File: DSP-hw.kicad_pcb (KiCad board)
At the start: 2 copper layers, 0 parts

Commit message: Iniziata un po la schematica
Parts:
- added C1: 100n, Capacitor_SMD:C_0603_1608Metric, F.Cu at (136.6, 67.8)
- added C10: 10u, Capacitor_SMD:C_0603_1608Metric, F.Cu at (136.6, 90.3)
- added C11: 1u, Capacitor_SMD:C_0603_1608Metric, F.Cu at (136.6, 92.9)
- added C12: 100n, Capacitor_SMD:C_0603_1608Metric, F.Cu at (136.6, 95.4)
- added C13: 10u, Capacitor_SMD:C_0603_1608Metric, F.Cu at (140.6, 67.8)
- added C14: 100n, Capacitor_SMD:C_0603_1608Metric, F.Cu at (140.6, 70.3)
- added C15: 10u, Capacitor_SMD:C_0603_1608Metric, F.Cu at (140.6, 72.8)
- added C16: 100n, Capacitor_SMD:C_0603_1608Metric, F.Cu at (140.6, 75.3)
- added C17: 10u, Capacitor_SMD:C_0603_1608Metric, F.Cu at (140.6, 77.8)
- added C18: 100n, Capacitor_SMD:C_0603_1608Metric, F.Cu at (140.6, 80.3)
- added C19: 47u, Capacitor_SMD:C_0603_1608Metric, F.Cu at (140.6, 82.8)
- added C2: 10u, Capacitor_SMD:C_0603_1608Metric, F.Cu at (136.6, 70.3)
- added C20: 47u, Capacitor_SMD:C_0603_1608Metric, F.Cu at (140.6, 85.3)
- added C21: 100n, Capacitor_SMD:C_0603_1608Metric, F.Cu at (140.6, 87.8)
- added C22: 22p, Capacitor_SMD:C_0603_1608Metric, F.Cu at (140.6, 90.3)
- added C23: 22p, Capacitor_SMD:C_0603_1608Metric, F.Cu at (140.6, 92.9)
- added C24: 10u, Capacitor_SMD:C_0603_1608Metric, F.Cu at (140.6, 95.4)
- added C25: 10u, Capacitor_SMD:C_0603_1608Metric, F.Cu at (144.6, 67.8)
- added C26: 10u, Capacitor_SMD:C_0603_1608Metric, F.Cu at (144.6, 70.3)
- added C27: 56n, Capacitor_SMD:C_0603_1608Metric, F.Cu at (144.6, 72.8)
- added C28: 56n, Capacitor_SMD:C_0603_1608Metric, F.Cu at (144.6, 75.3)
- added C29: 10u, Capacitor_SMD:C_0603_1608Metric, F.Cu at (144.6, 77.8)
- added C3: 100n, Capacitor_SMD:C_0603_1608Metric, F.Cu at (136.6, 72.8)
- added C30: 56n, Capacitor_SMD:C_0603_1608Metric, F.Cu at (144.6, 80.3)
- added C31: 56n, Capacitor_SMD:C_0603_1608Metric, F.Cu at (144.6, 82.8)
- added C32: 10u, Capacitor_SMD:C_0603_1608Metric, F.Cu at (144.6, 85.3)
- added C33: 56n, Capacitor_SMD:C_0603_1608Metric, F.Cu at (144.6, 87.8)
- added C34: 56n, Capacitor_SMD:C_0603_1608Metric, F.Cu at (144.6, 90.3)
- added C35: 10u, Capacitor_SMD:C_0603_1608Metric, F.Cu at (144.6, 92.9)
- added C36: 56n, Capacitor_SMD:C_0603_1608Metric, F.Cu at (144.6, 95.4)
- added C37: 56n, Capacitor_SMD:C_0603_1608Metric, F.Cu at (148.6, 67.8)
- added C38: 100n, Capacitor_SMD:C_0603_1608Metric, F.Cu at (148.6, 70.3)
- added C39: 1u, Capacitor_SMD:C_0603_1608Metric, F.Cu at (148.6, 72.8)
- added C4: 10u, Capacitor_SMD:C_0603_1608Metric, F.Cu at (136.6, 75.3)
- added C40: 22u, Capacitor_SMD:C_0603_1608Metric, F.Cu at (148.6, 75.3)
- added C41: 100n, Capacitor_SMD:C_0603_1608Metric, F.Cu at (148.6, 77.8)
- added C5: 10u, Capacitor_SMD:C_0603_1608Metric, F.Cu at (136.6, 77.8)
- added C6: 100n, Capacitor_SMD:C_0603_1608Metric, F.Cu at (136.6, 80.3)
- added C7: 1u, Capacitor_SMD:C_0603_1608Metric, F.Cu at (136.6, 82.8)
- added C8: 10u, Capacitor_SMD:C_0603_1608Metric, F.Cu at (136.6, 85.3)
- added C9: 100n, Capacitor_SMD:C_0603_1608Metric, F.Cu at (136.6, 87.8)
- added J1: XLR3_AudioJack3_Combo_Ground, Connector_Audio:Jack_XLR-6.35mm_Neutrik_NCJ6FA-H-0_Horizontal, F.Cu at (109.5, 73.0)
- added J2: NC3MAH, Connector_Audio:Jack_XLR_Neutrik_NC3MAH_Horizontal, F.Cu at (85.0, 69.2)
- added J3: NC3MAH, Connector_Audio:Jack_XLR_Neutrik_NC3MAH_Horizontal, F.Cu at (85.0, 93.5)
- added J4: NC3MAH, Connector_Audio:Jack_XLR_Neutrik_NC3MAH_Horizontal, F.Cu at (85.0, 117.7)
- added J5: NC3MAH, Connector_Audio:Jack_XLR_Neutrik_NC3MAH_Horizontal, F.Cu at (85.0, 141.9)
- added J6: XLR3_AudioJack3_Combo_Ground, Connector_Audio:Jack_XLR-6.35mm_Neutrik_NCJ6FA-H-0_Horizontal, F.Cu at (109.5, 100.1)
- added J7: USB_C_Receptacle_USB2.0_16P, Connector_USB:USB_C_Receptacle_GCT_USB4085, F.Cu at (152.0, 98.2)
- added J8: Conn_01x04_Pin, Connector_JST:JST_XH_B4B-XH-AM_1x04_P2.50mm_Vertical, F.Cu at (138.1, 106.7)
- added Q1: BC327, Package_TO_SOT_THT:TO-92_Inline, F.Cu at (162.5, 117.7)
- added R1: 1k, Resistor_SMD:R_0603_1608Metric, F.Cu at (148.6, 80.3)
- added R10: 10k, Resistor_SMD:R_0603_1608Metric, F.Cu at (152.7, 72.8)
- added R11: 47k, Resistor_SMD:R_0603_1608Metric, F.Cu at (152.7, 75.3)
- added R12: 10k, Resistor_SMD:R_0603_1608Metric, F.Cu at (152.7, 77.8)
- added R13: 33, Resistor_SMD:R_0603_1608Metric, F.Cu at (152.7, 80.3)
- added R14: 47k, Resistor_SMD:R_0603_1608Metric, F.Cu at (152.7, 82.8)
- added R15: 47k, Resistor_SMD:R_0603_1608Metric, F.Cu at (152.7, 85.3)
- added R16: 33, Resistor_SMD:R_0603_1608Metric, F.Cu at (152.7, 87.8)
- added R17: 47k, Resistor_SMD:R_0603_1608Metric, F.Cu at (152.7, 90.3)
- added R18: 47k, Resistor_SMD:R_0603_1608Metric, F.Cu at (152.7, 92.9)
- added R19: 33, Resistor_SMD:R_0603_1608Metric, F.Cu at (152.7, 95.4)
- added R2: 33, Resistor_SMD:R_0603_1608Metric, F.Cu at (148.6, 82.8)
- added R20: 47k, Resistor_SMD:R_0603_1608Metric, F.Cu at (156.7, 67.8)
- added R21: 47k, Resistor_SMD:R_0603_1608Metric, F.Cu at (156.7, 70.3)
- added R22: 33, Resistor_SMD:R_0603_1608Metric, F.Cu at (156.7, 72.8)
- added R23: 47k, Resistor_SMD:R_0603_1608Metric, F.Cu at (156.7, 75.3)
- added R24: 47k, Resistor_SMD:R_0603_1608Metric, F.Cu at (156.7, 77.8)
- added R25: 5.1k, Resistor_SMD:R_0603_1608Metric, F.Cu at (156.7, 80.3)
- added R26: 5.1k, Resistor_SMD:R_0603_1608Metric, F.Cu at (156.7, 82.8)
- added R27: 10k, Capacitor_SMD:C_0603_1608Metric, F.Cu at (156.7, 85.3)
- added R28: 4k7, Resistor_SMD:R_0603_1608Metric, F.Cu at (156.5, 90.8)
- added R29: 4k7, Resistor_SMD:R_0603_1608Metric, F.Cu at (156.7, 87.8)
- added R3: 33, Resistor_SMD:R_0603_1608Metric, F.Cu at (148.6, 85.3)
- added R4: 2k2, Resistor_SMD:R_0603_1608Metric, F.Cu at (148.6, 87.8)
- added R5: 18k, Resistor_SMD:R_0603_1608Metric, F.Cu at (148.6, 90.3)
- added R6: 100, Resistor_SMD:R_0603_1608Metric, F.Cu at (148.6, 92.9)
- added R7: 33, Resistor_SMD:R_0603_1608Metric, F.Cu at (148.6, 95.4)
- added R8: 10k, Resistor_SMD:R_0603_1608Metric, F.Cu at (152.7, 67.8)
- added R9: 47k, Resistor_SMD:R_0603_1608Metric, F.Cu at (152.7, 70.3)
- added SW1: SW_Push, Button_Switch_SMD:SW_SPST_PTS645Sx43SMTR92, F.Cu at (164.2, 70.4)
- added SW2: SW_SPST, Button_Switch_THT:SW_DIP_SPSTx01_Slide_9.78x4.72mm_W7.62mm_P2.54mm, F.Cu at (153.8, 123.8)
- added SW3: SW_SPST, Button_Switch_THT:SW_DIP_SPSTx01_Slide_9.78x4.72mm_W7.62mm_P2.54mm, F.Cu at (153.8, 130.2)
- added SW4: SW_SPST, Button_Switch_THT:SW_DIP_SPSTx01_Slide_9.78x4.72mm_W7.62mm_P2.54mm, F.Cu at (153.8, 136.7)
- added SW5: SW_SPST, Button_Switch_THT:SW_DIP_SPSTx01_Slide_9.78x4.72mm_W7.62mm_P2.54mm, F.Cu at (153.8, 143.1)
- added SW6: SW_SPST, Button_Switch_THT:SW_DIP_SPSTx01_Slide_9.78x4.72mm_W7.62mm_P2.54mm, F.Cu at (153.8, 149.5)
- added SW7: SW_SPST, Button_Switch_THT:SW_DIP_SPSTx01_Slide_9.78x4.72mm_W7.62mm_P2.54mm, F.Cu at (153.8, 155.9)
- added SW8: SW_Push, Button_Switch_SMD:SW_SPST_PTS645Sx43SMTR92, F.Cu at (164.2, 78.3)
- added U1: ADAU1701, Package_QFP:LQFP-48_7x7mm_P0.5mm, F.Cu at (154.9, 113.5)
- added U2: CAT24C256, Package_SO:SOIC-8_3.9x4.9mm_P1.27mm, F.Cu at (164.8, 111.2)
- added U3: AMS1117-3.3, Package_TO_SOT_SMD:SOT-223-3_TabPin2, F.Cu at (139.5, 115.4)
- added U4: ESP32-S3-WROOM-2, RF_Module:ESP32-S3-WROOM-2, F.Cu at (127.1, 149.1)
- added Y1: 12.228M, Crystal:Crystal_SMD_HC49-SD, F.Cu at (141.9, 100.0)

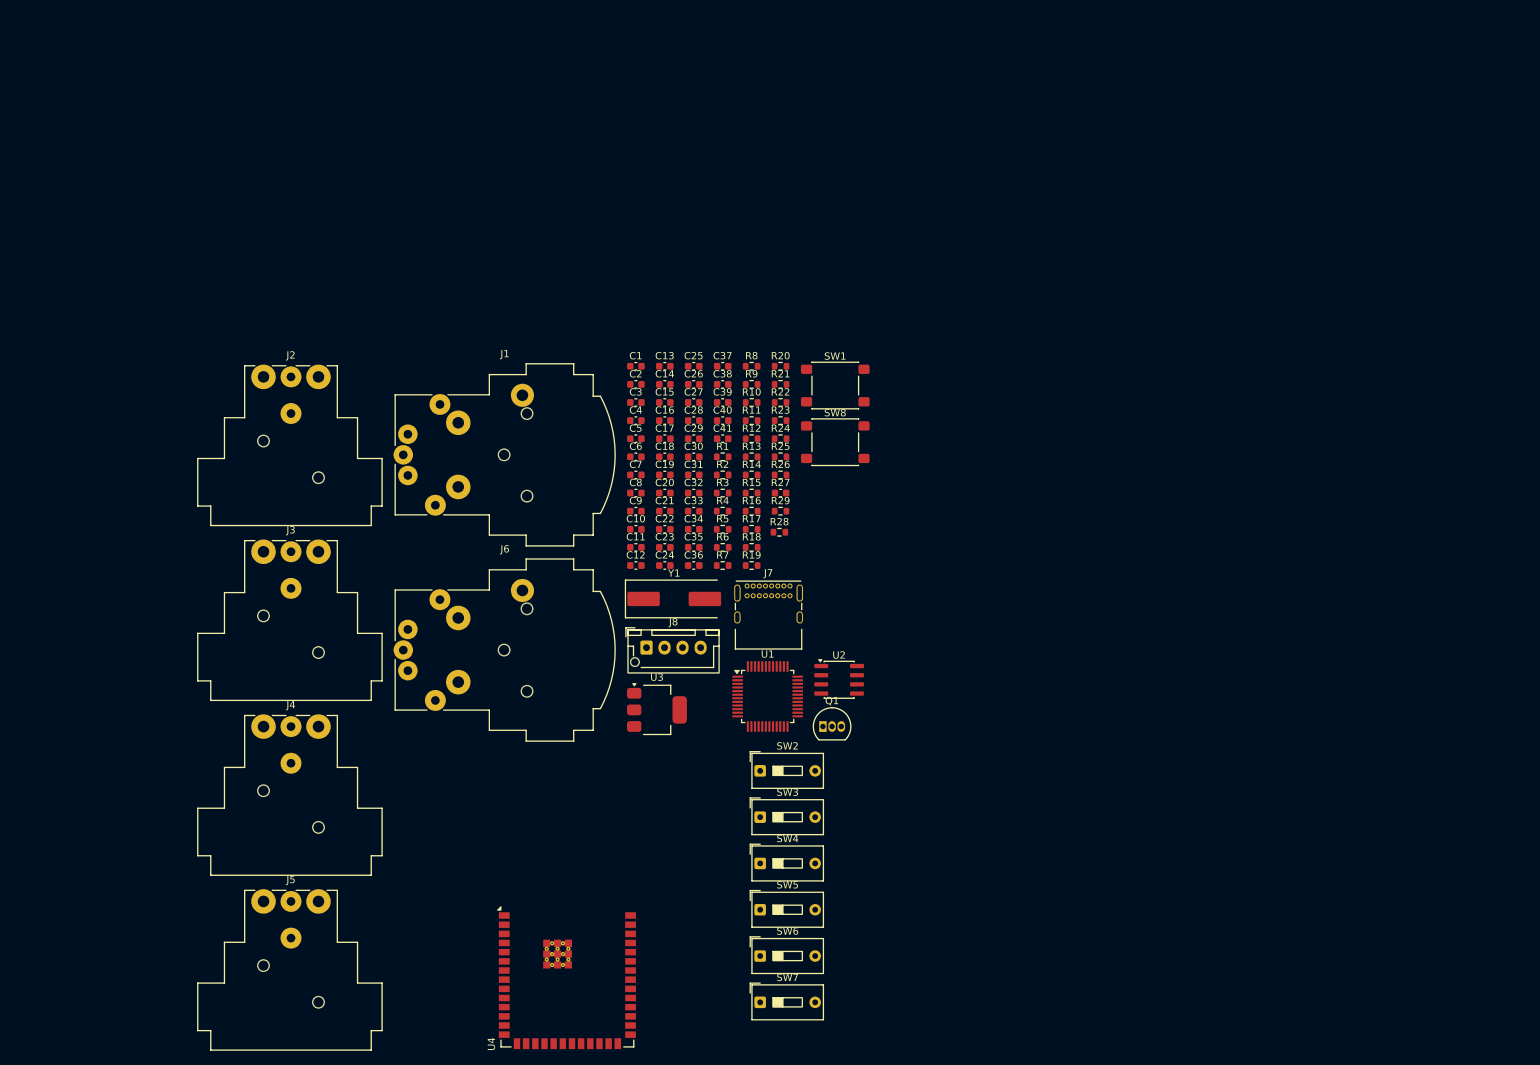
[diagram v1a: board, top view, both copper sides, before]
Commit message: aggiunto filtro PLL_LF Adau
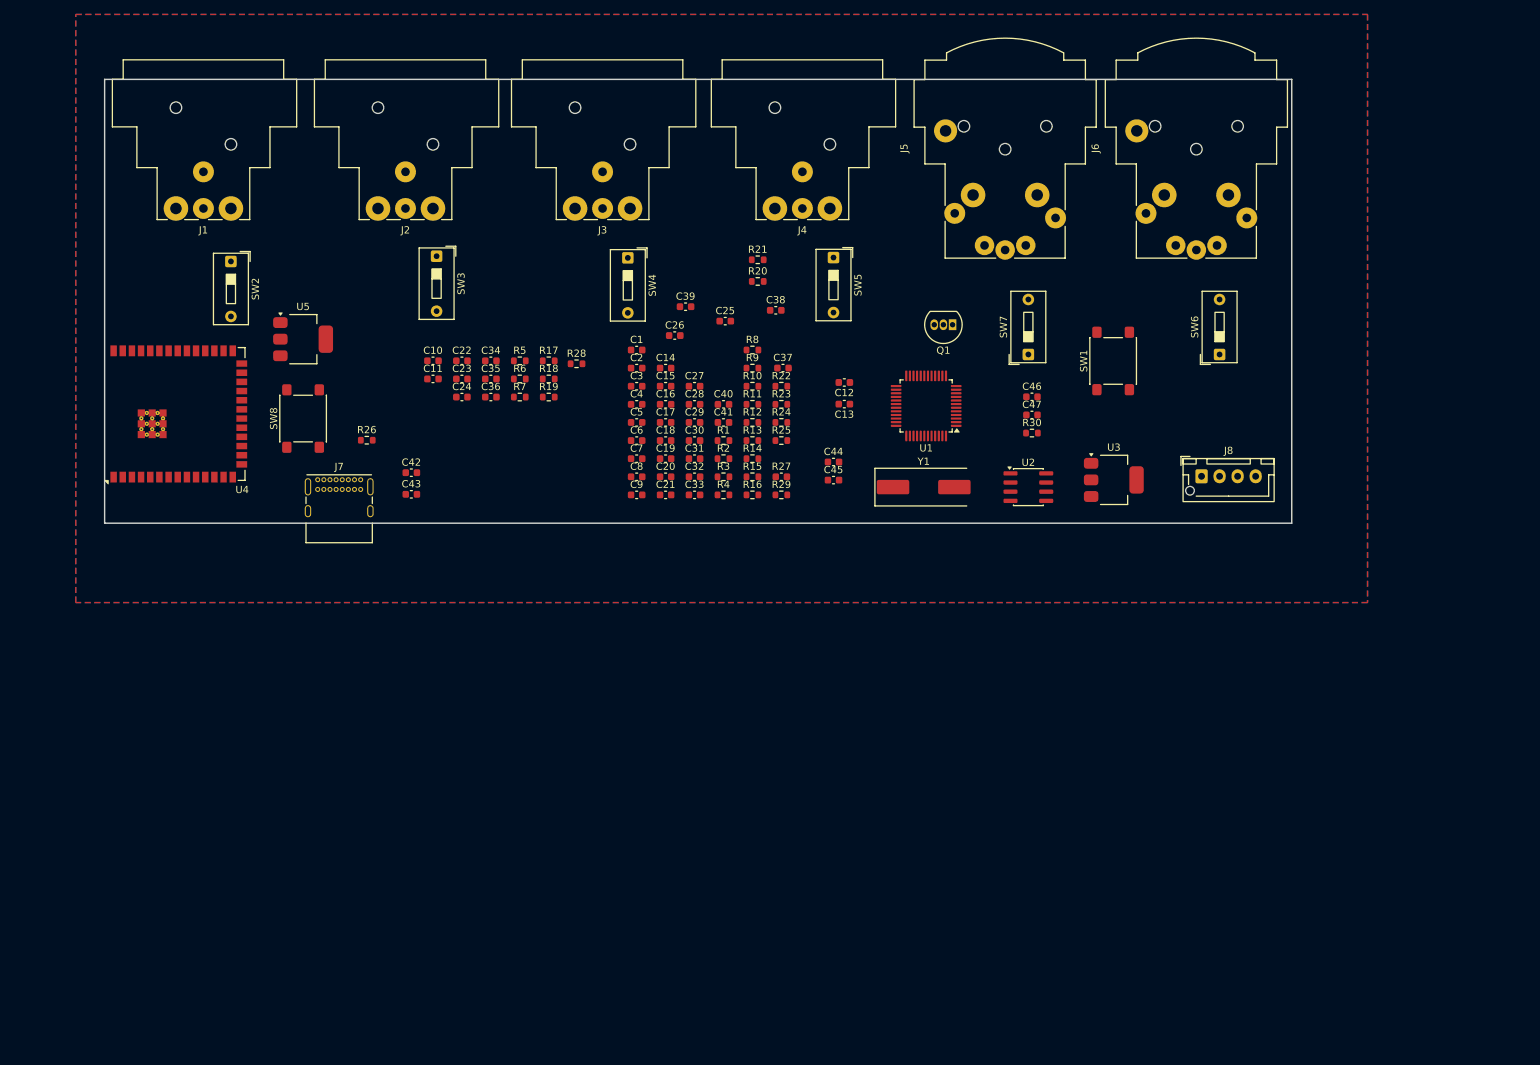
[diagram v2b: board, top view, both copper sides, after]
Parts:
- added C42: 100n, Capacitor_SMD:C_0603_1608Metric, F.Cu at (105.5, 82.5)
- added C43: 47u, Capacitor_SMD:C_0603_1608Metric, F.Cu at (105.5, 85.5)
- added C44: 100n, Capacitor_SMD:C_0603_1608Metric, F.Cu at (164.0, 81.0)
- added C45: 47u, Capacitor_SMD:C_0603_1608Metric, F.Cu at (164.0, 83.5)
- added C46: 3.3n, Capacitor_SMD:C_0603_1608Metric, F.Cu at (191.5, 72.0)
- added C47: 56n, Capacitor_SMD:C_0603_1608Metric, F.Cu at (191.5, 74.5)
- added R30: 475, Resistor_SMD:R_0603_1608Metric, F.Cu at (191.5, 77.0)
- added U5: AMS1117-3.3, Package_TO_SOT_SMD:SOT-223-3_TabPin2, F.Cu at (90.5, 64.0)
- moved J4 124.0 mm to (163.5, 45.9), turned to 180 degrees
- moved SW6 104.9 mm to (217.5, 66.1), turned to 90 degrees
- moved SW2 101.8 mm to (80.5, 53.2), turned to -90 degrees
- moved J6 101.4 mm to (207.3, 46.6), turned to 90 degrees
- moved SW7 97.2 mm to (191.0, 66.1), turned to 90 degrees
- moved U4 94.4 mm to (69.5, 74.4), turned to 90 degrees
- moved SW5 90.9 mm to (164.0, 52.7), turned to -90 degrees
- moved SW3 89.7 mm to (109.0, 52.5), turned to -90 degrees
- moved J5 89.2 mm to (180.8, 46.6), turned to 90 degrees
- moved J3 87.9 mm to (135.8, 45.9), turned to 180 degrees
- moved SW4 85.9 mm to (135.5, 52.7), turned to -90 degrees
- moved J8 80.5 mm to (215.0, 83.0)
- moved SW8 73.8 mm to (90.5, 75.0), turned to 90 degrees
- moved U3 70.9 mm to (202.8, 83.5)
- moved J7 61.3 mm to (92.5, 83.5)
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- renumbered J2 to J1, J3 to J2, J4 to J3, J5 to J4, J6 to J5, J1 to J6
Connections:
- R10 pad 1: /Input Output filter/ADC0 -> /Input Output filter/ADC1
- R12 pad 1: /Input Output filter/ADC1 -> /Input Output filter/ADC0
- U1 pad 35: unconnected-(U1-PLL_LF-Pad35) -> /DSP-hw/PLL_LF
- U4 pad 2: +3V3 -> Net-(U4-3V3)
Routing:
- added copper zone on B.Cu, net GND
- added copper zone on F.Cu, net GND
- added copper zone on In1.Cu, net GND
- added copper zone on In2.Cu, net GND
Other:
- board outline added: 164.5 x 61.5 mm
- copper layers 2 -> 4
